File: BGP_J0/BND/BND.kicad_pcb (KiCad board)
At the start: 2 copper layers, 25 x 28 mm, 7 parts, among them J1 Conn_01x13, J2 Conn_01x03, J3 Conn_01x02, J4 Conn_01x02, J5 Conn_01x03, J6 Conn_01x02, J7 Conn_01x02

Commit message: J0 - Panelisation
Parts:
- moved J1 0.10 mm to (112.5, 71.6)
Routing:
- net /BT_O: track 10.5 -> 12.6 mm
- net /V_I: track 10.5 -> 11.2 mm

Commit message: Gerbers fixed - ready to go
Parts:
- removed J3, J6: Conn_01x02, LIBS:TerminalBlock_Phoenix_MPT-2.54mm_2pol
- removed J7: Conn_01x02, Connectors_JST:JST_PH_B2B-PH-K_02x2.00mm_Straight
- added P7: CONN_01X04, Connectors_JST:JST_PH_B4B-PH-K_04x2.00mm_Straight, F.Cu at (107.3, 87.8)
- moved J4 0.10 mm to (127.7, 81.8)
- moved J1 0.10 mm to (112.5, 71.5)
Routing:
- net /B_+: track 22.2 -> 18.6 mm

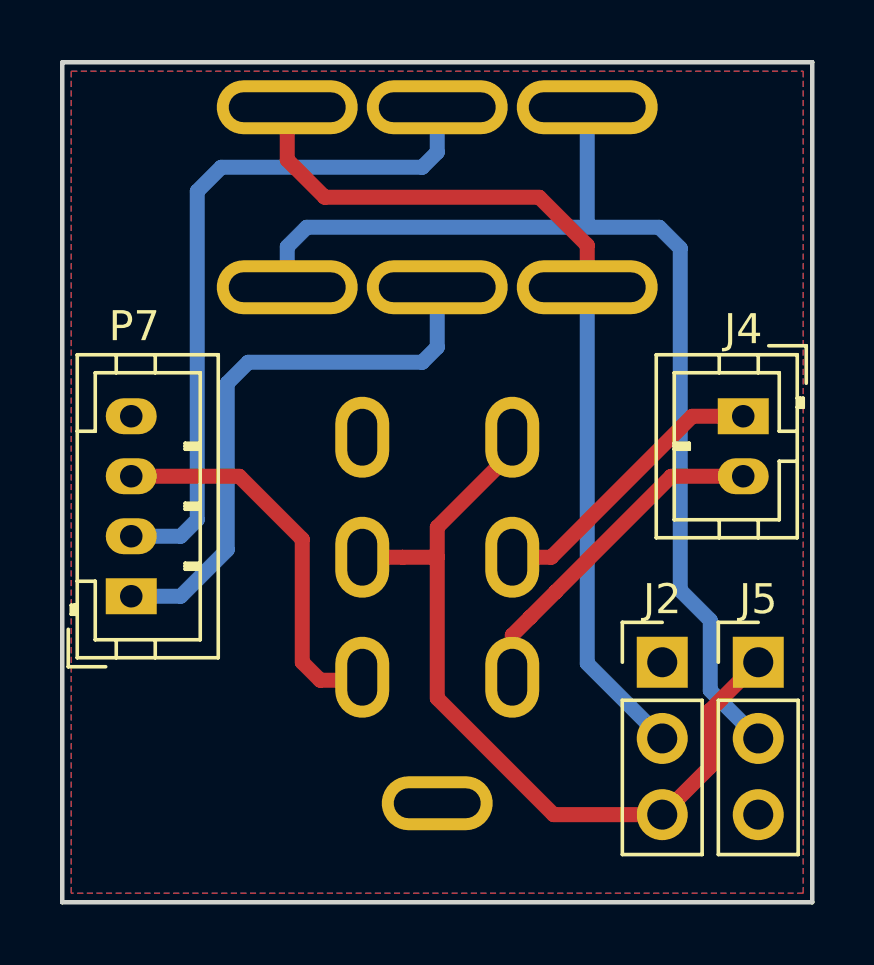
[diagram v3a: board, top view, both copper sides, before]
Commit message: Ready to go
Reverted J0_BND  to include P/U inputs
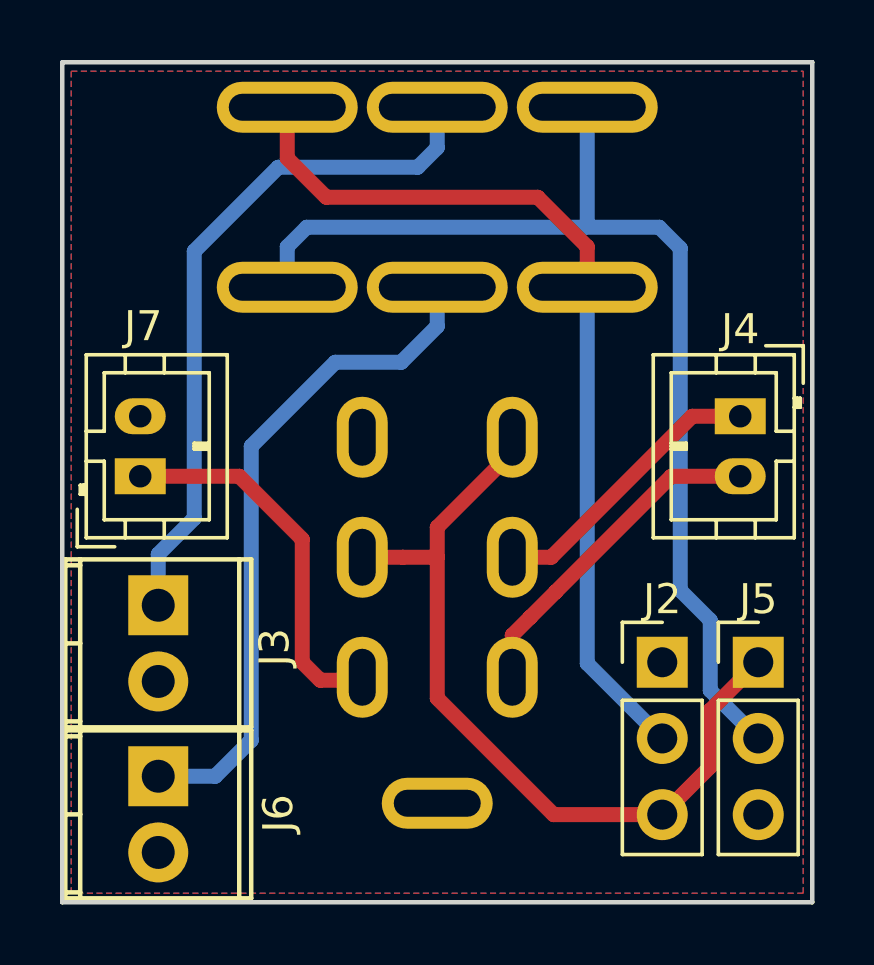
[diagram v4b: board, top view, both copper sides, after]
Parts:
- removed P7: CONN_01X04, Connectors_JST:JST_PH_B4B-PH-K_04x2.00mm_Straight
- added J3: Conn_01x02, LIBS:TerminalBlock_Phoenix_MPT-2.54mm_2pol, F.Cu at (108.2, 88.1)
- added J6: Conn_01x02, LIBS:TerminalBlock_Phoenix_MPT-2.54mm_2pol, F.Cu at (108.2, 93.8)
- added J7: Conn_01x02, Connectors_JST:JST_PH_B2B-PH-K_02x2.00mm_Straight, F.Cu at (107.6, 83.8)
- moved J4 0.10 mm to (127.6, 81.8)
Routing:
- net /B_+: track 18.6 -> 22.6 mm
